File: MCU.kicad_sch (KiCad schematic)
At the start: 20 parts, among them J1 USB_C_Receptacle, J3 Conn_01x06, SW3 SW_Push, SW4 SW_Push, SW5 SW_Push, SW6 SW_Push, U11 ESDR0502NMUTBG, U7 LSF0204GU12X, U8 FAN5622SX, U9 NORA-B106-00B, X1 Q13FC1350000400, X608 Display

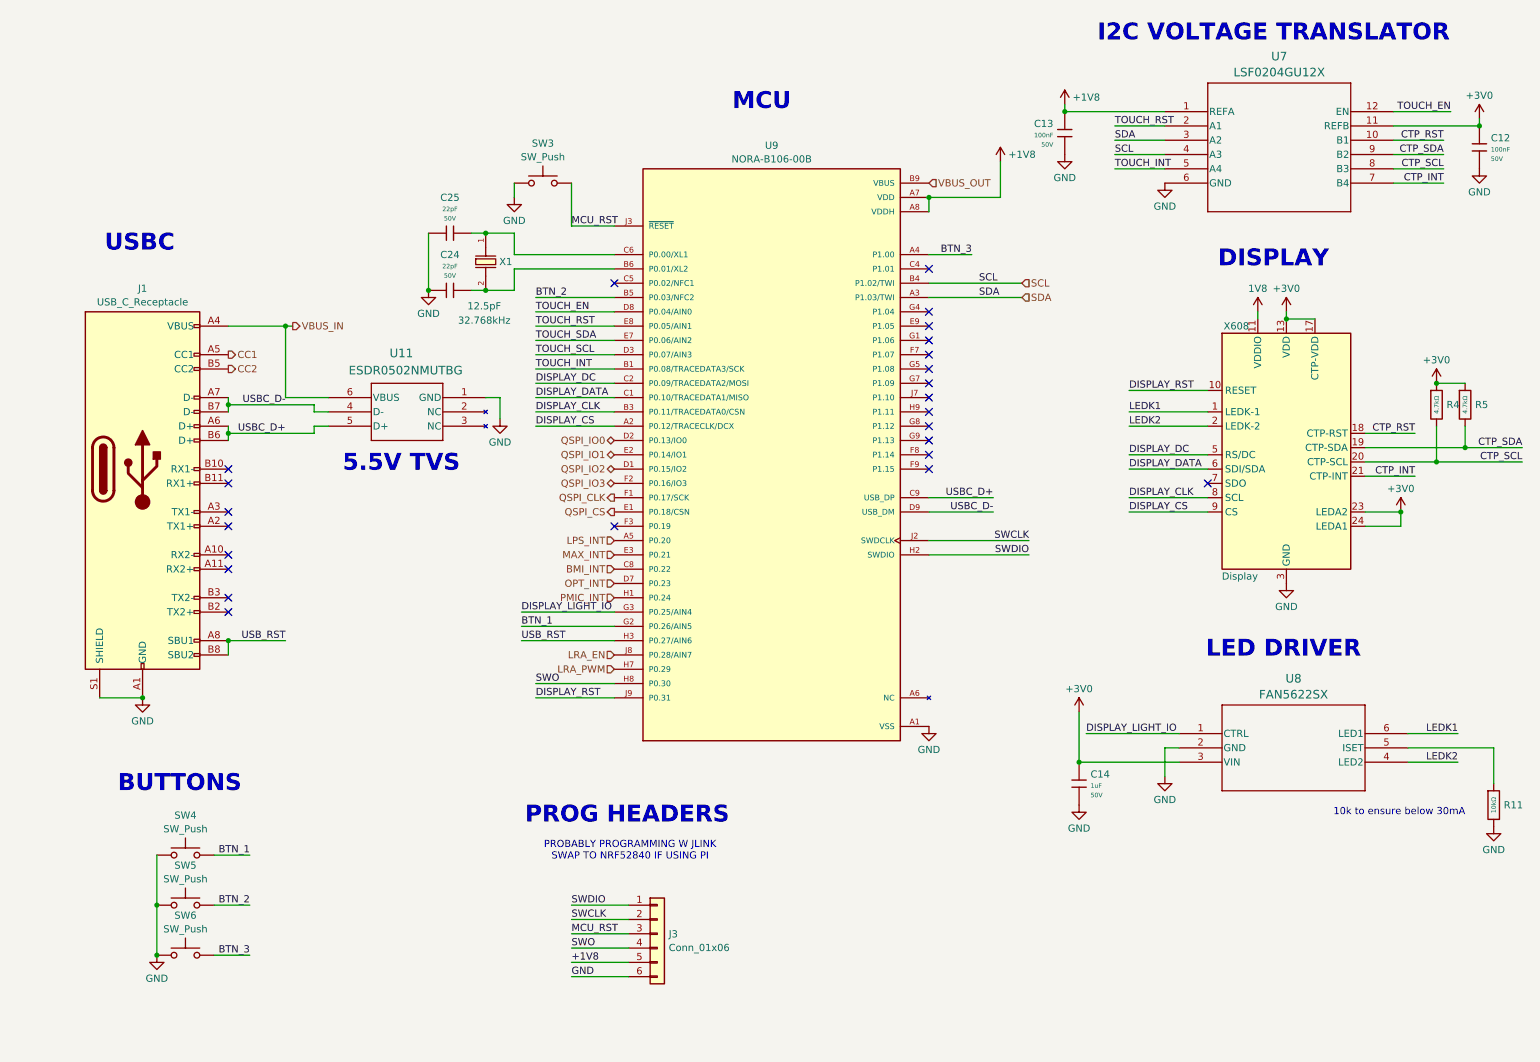
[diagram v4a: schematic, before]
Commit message: Updated Schem and Organized Layout
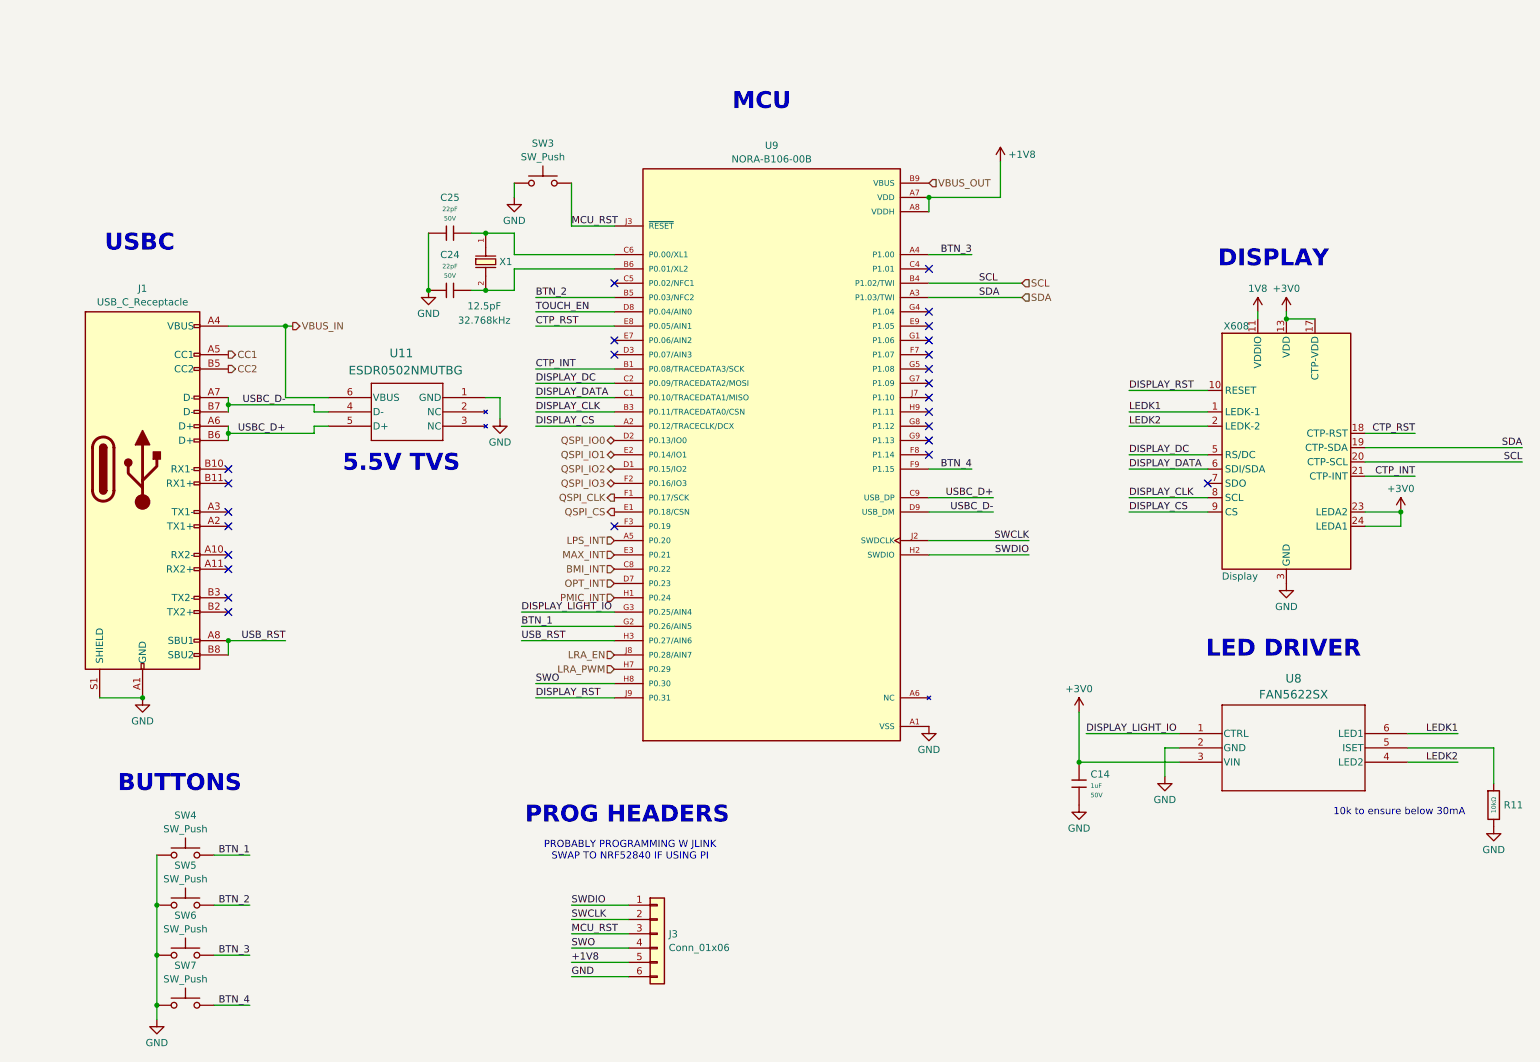
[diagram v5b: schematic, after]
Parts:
- removed C12, C13: 100nF, PCM_JLCPCB:C_0603, symbol PCM_JLCPCB-Capacitors:0603,100nF
- removed R4, R5: 4.7kΩ, PCM_JLCPCB:R_0603, symbol PCM_JLCPCB-Resistors:0603,4.7kΩ
- removed U7: LSF0204GU12X, XQFN12_SOT1174-1_NEX, symbol 2026-04-09_00-54-12:LSF0204GU12X
- added SW7: SW_Push, Button_Switch_SMD:SW_Push_1P1T-MP_NO_Horizontal_Alps_SKRTLAE010, symbol Switch:SW_Push
- C14, C24, C25: Manufacturer Samsung Electro-Mechanics -> (none)
- J1: footprint (none) -> Connector_USB:USB_C_Receptacle_Amphenol_12401548E4-2A
- J3: footprint (none) -> PAD_CONNECTOR:2x03_1x1mm
- R11: Manufacturer UNI-ROYAL(Uniroyal Elec) -> (none)
- SW3: footprint (none) -> SKRPACE:SW_SKRPACE010_AAL
- SW4, SW5, SW6: footprint (none) -> Button_Switch_SMD:SW_Push_1P1T-MP_NO_Horizontal_Alps_SKRTLAE010
- U11: footprint UDFN6_517AA_ONS -> ESD:UDFN6_517AA_ONS
- U8: footprint SSOT6_3X1P7_ONS -> FAN:SSOT6_3X1P7_ONS
- X1: Manufacturer Seiko Epson -> (none)
- X608: footprint EastRising:ER-CON0.4-24P -> ZIF:24-PIN-ZIF
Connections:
- net CTP_SCL is gone; now on net SCL: X608.20 (CTP-SCL)
- net CTP_SDA is gone; now on net SDA: X608.19 (CTP-SDA)
- net TOUCH_INT is gone; now on net CTP_INT: U9.B1 (P0.08/TRACEDATA3/SCK)
- net TOUCH_RST is gone; now on net CTP_RST: U9.E8 (P0.05/AIN1)
- net GND: now also SW7.1
- net BTN_4: now reaches U9.F9 (P1.15)
- net BTN_4: now also SW7.2
- net TOUCH_SCL: no longer names the net of U9.D3 (P0.07/AIN3)
- net TOUCH_SDA: no longer names the net of U9.E7 (P0.06/AIN2)
- no-connect marks 24 -> 25
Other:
- note removed: "I2C VOLTAGE TRANSLATOR"

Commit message: Layout V1
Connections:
- net CLK1: now reaches C25.2, U9.C6 (P0.00/XL1), X1.1
- net CLK2: now reaches C24.2, U9.B6 (P0.01/XL2), X1.2
- net ISET: now reaches R11.1, U8.5 (ISET)
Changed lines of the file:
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@@
+		)
+	)
+	(label "ISET"
+		(at 266.7 143.51 0)
+		(effects
+			(font
+				(size 1.27 1.27)
+			)
+			(justify left bottom)
 		)
 	)
@@
 		)
 	)
+	(label "CLK1"
+		(at 113.03 55.88 0)
+		(effects
+			(font
+				(size 1.27 1.27)
+			)
+			(justify left bottom)
+		)
+	)
 	(label "DISPLAY_DC"
 		(at 213.36 91.44 0)
@@
 		(effects
 			(font
+				(size 1.27 1.27)
+			)
+			(justify left bottom)
+		)
+	)
+	(label "CLK2"
+		(at 113.03 58.42 0)
+		(effects
+			(font

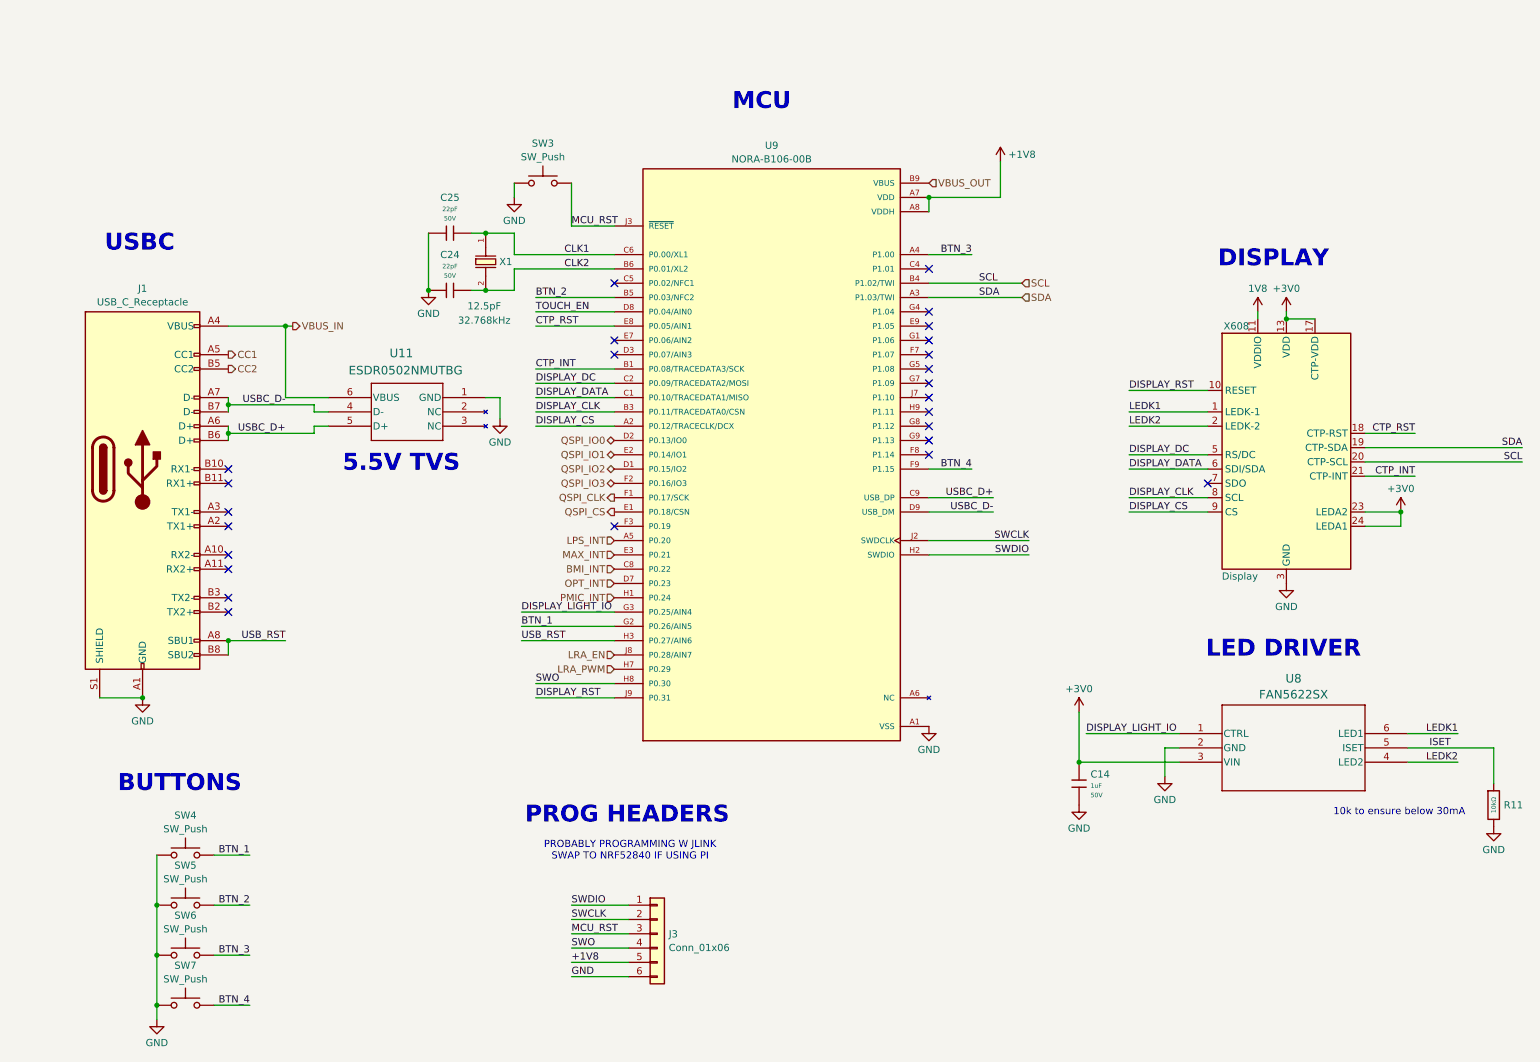
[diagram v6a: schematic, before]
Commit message: Update most sym/footprint libraries
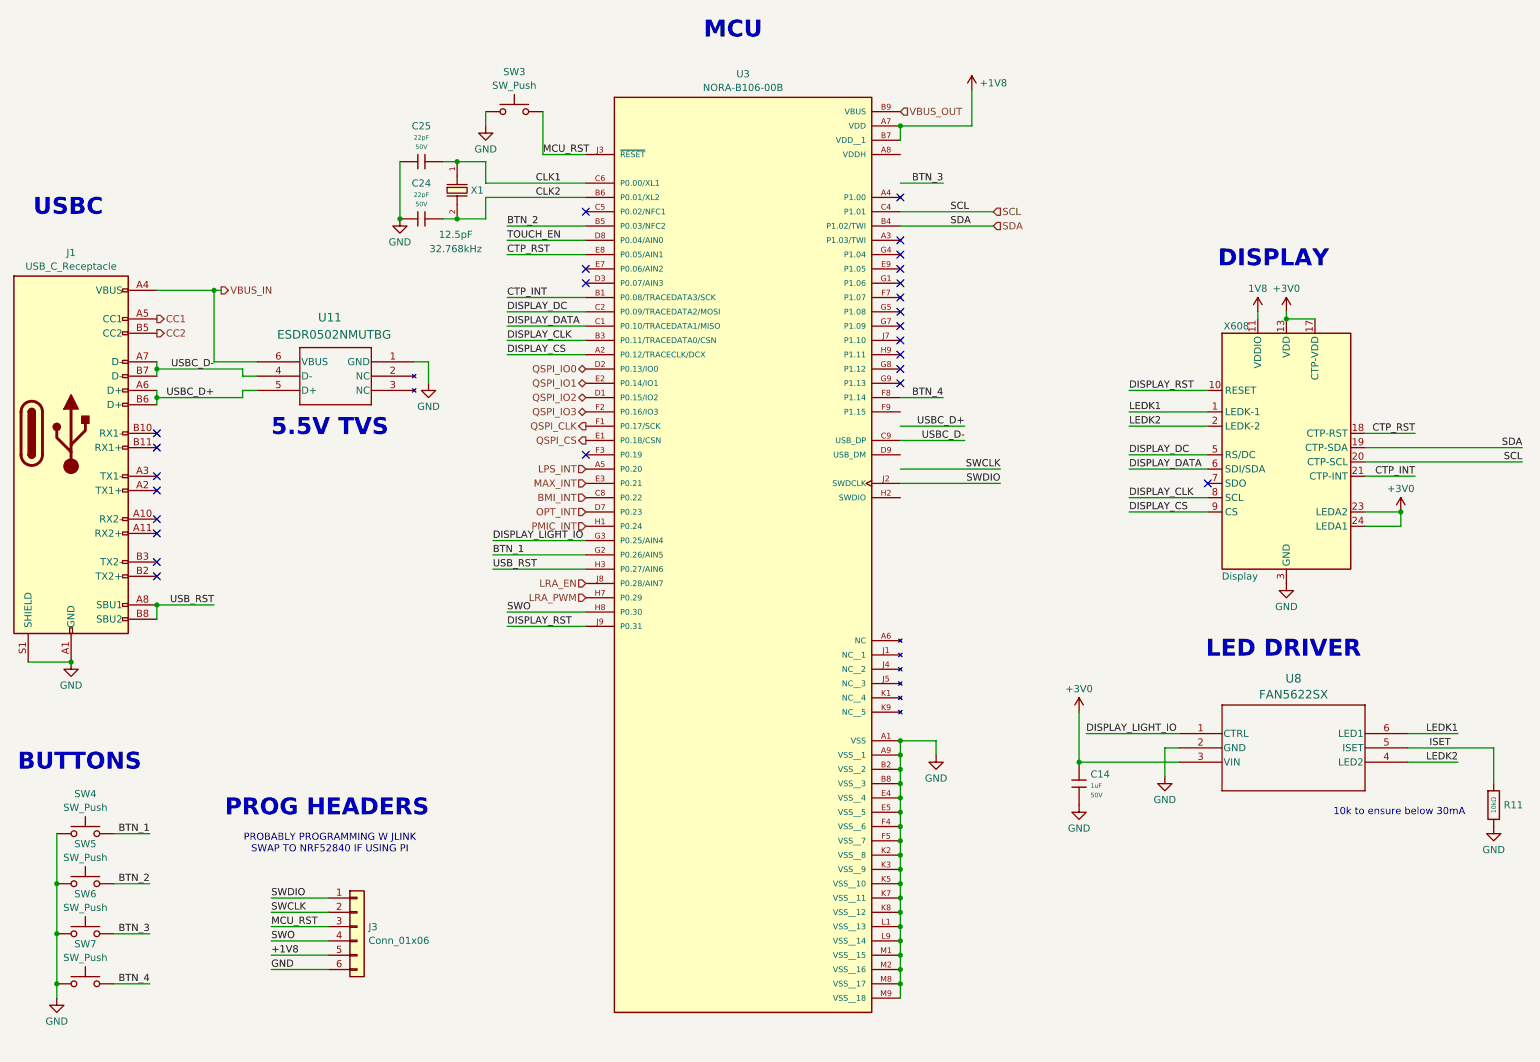
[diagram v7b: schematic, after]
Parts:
- removed U9: NORA-B106-00B, NORA-B106-00B:XCVR_NORA-B106-00B, symbol NORA-B106-00B:NORA-B106-00B
- added U3: NORA-B106-00B, Smart_Watch:XCVR_NORA-B106-00B, symbol Smart_Watch:NORA-B106-00B
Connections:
- net +1V8: now also U3.A7 (VDD), U3.B7 (VDD__1)
- net BMI_INT: now also U3.C8 (P0.22)
- net BTN_1: now also U3.G2 (P0.26/AIN5)
- net BTN_2: now also U3.B5 (P0.03/NFC2)
- net BTN_4: now also U3.F8 (P1.14)
- net CLK1: now also U3.C6 (P0.00/XL1)
- net CLK2: now also U3.B6 (P0.01/XL2)
- net CTP_INT: now also U3.B1 (P0.08/TRACEDATA3/SCK)
- net CTP_RST: now also U3.E8 (P0.05/AIN1)
- net DISPLAY_CLK: now also U3.B3 (P0.11/TRACEDATA0/CSN)
- net DISPLAY_CS: now also U3.A2 (P0.12/TRACECLK/DCX)
- net DISPLAY_DATA: now also U3.C1 (P0.10/TRACEDATA1/MISO)
- net DISPLAY_DC: now also U3.C2 (P0.09/TRACEDATA2/MOSI)
- net DISPLAY_LIGHT_IO: now also U3.G3 (P0.25/AIN4)
- net DISPLAY_RST: now also U3.J9 (P0.31)
- net GND: now also U3.A1 (VSS), U3.A9 (VSS__1), U3.B2 (VSS__2), U3.B8 (VSS__3), U3.E4 (VSS__4), U3.E5 (VSS__5), U3.F4 (VSS__6), U3.F5 (VSS__7), U3.K2 (VSS__8), U3.K3 (VSS__9), U3.K5 (VSS__10), U3.K7 (VSS__11), U3.K8 (VSS__12), U3.L1 (VSS__13), U3.L9 (VSS__14), U3.M1 (VSS__15), U3.M2 (VSS__16), U3.M8 (VSS__17), U3.M9 (VSS__18)
- net LPS_INT: now also U3.A5 (P0.20)
- net LRA_EN: now also U3.J8 (P0.28/AIN7)
- net LRA_PWM: now also U3.H7 (P0.29)
- net MAX_INT: now also U3.E3 (P0.21)
- net MCU_RST: now also U3.J3 (~{RESET})
- net OPT_INT: now also U3.D7 (P0.23)
- net PMIC_INT: now also U3.H1 (P0.24)
- net QSPI_CLK: now also U3.F1 (P0.17/SCK)
- net QSPI_CS: now also U3.E1 (P0.18/CSN)
- net QSPI_IO0: now also U3.D2 (P0.13/IO0)
- net QSPI_IO1: now also U3.E2 (P0.14/IO1)
- net QSPI_IO2: now also U3.D1 (P0.15/IO2)
- net QSPI_IO3: now also U3.F2 (P0.16/IO3)
- net SCL: now also U3.C4 (P1.01)
- net SDA: now also U3.B4 (P1.02/TWI)
- net SWDIO: now also U3.J2 (SWDCLK)
- net SWO: now also U3.H8 (P0.30)
- net TOUCH_EN: now also U3.D8 (P0.04/AIN0)
- net USBC_D-: now also U3.C9 (USB_DP)
- net USB_RST: now also U3.H3 (P0.27/AIN6)
- net VBUS_OUT: now also U3.B9 (VBUS)
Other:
- moved on the sheet: C24, C25, J1, J3, SW3, SW4, SW5, SW6, SW7, U11, X1

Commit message: Change more footprints
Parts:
- SW4, SW5, SW6, SW7: footprint Button_Switch_SMD:SW_Push_1P1T-MP_NO_Horizontal_Alps_SKRTLAE010 -> Smart_Watch:SW_Push_1P1T-MP_NO_Horizontal_Alps_SKRTLAE010_3D
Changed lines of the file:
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@@
 			)
 		)
-		(property "Footprint" "Button_Switch_SMD:SW_Push_1P1T-MP_NO_Horizontal_Alps_SKRTLAE010"
+		(property "Footprint" "Smart_Watch:SW_Push_1P1T-MP_NO_Horizontal_Alps_SKRTLAE010_3D"
 			(at 27.94 180.34 0)
 			(hide yes)
@@
 			)
 		)
-		(property "Footprint" "Button_Switch_SMD:SW_Push_1P1T-MP_NO_Horizontal_Alps_SKRTLAE010"
+		(property "Footprint" "Smart_Watch:SW_Push_1P1T-MP_NO_Horizontal_Alps_SKRTLAE010_3D"
 			(at 27.94 162.56 0)
 			(hide yes)
@@
 			)
 		)
-		(property "Footprint" "Button_Switch_SMD:SW_Push_1P1T-MP_NO_Horizontal_Alps_SKRTLAE010"
+		(property "Footprint" "Smart_Watch:SW_Push_1P1T-MP_NO_Horizontal_Alps_SKRTLAE010_3D"
 			(at 27.94 153.67 0)
 			(hide yes)
@@
 			)
 		)
-		(property "Footprint" "Button_Switch_SMD:SW_Push_1P1T-MP_NO_Horizontal_Alps_SKRTLAE010"
+		(property "Footprint" "Smart_Watch:SW_Push_1P1T-MP_NO_Horizontal_Alps_SKRTLAE010_3D"
 			(at 27.94 171.45 0)
 			(hide yes)
